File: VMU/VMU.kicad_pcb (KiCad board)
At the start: 4 copper layers, 76.2 x 53.3 mm, 62 parts, among them J1 TBL009-254-14GY-2GY, J2 TBL009-254-14GY-2GY, J3 Conn_01x08_Pin, J4 Conn_01x08_Pin, J5 Conn_01x02_Pin, J6 TBL009-254-14GY-2GY, J7 TBL009-254-14GY-2GY, J8 ARM_JTAG_SWD_10, Q1 NMOS, Q2 NMOS, Q3 NMOS, Q4 NMOS, Q6 NMOS, Q7 NMOS, U1 TLV9064, U2 TLV9064, U3 ADP150AUJZ-3.3-R7, U4 SN65HVD233, U5 STM32F091RCTx

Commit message: Labels
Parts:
- added G***: LOGO, LOGO, F.Cu at (127.0, 94.2)
- moved J5 2.25 mm to (104.5, 112.0)
- moved F3 2.00 mm to (104.8, 115.0)
- renumbered PWR to locked
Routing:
- net /PB_SUPPLY: track 58.5 -> 52.4 mm
- net GND: track 84.5 -> 81.5 mm
- net +5V: track 43.0 -> 41.2 mm

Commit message: Update
+ GND  vias
less silk screen
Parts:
- Hrt Beat: renamed from D6
- PB Supply: renamed from J5
- moved C2 1.25 mm to (141.5, 96.5)
- moved C1 1.00 mm to (141.2, 108.5)
- renumbered D7 to Error, Q2 to Q1, Q4 to Q2, Q6 to Q3, Q7 to Q4, Q1 to Q5, Q3 to Q6, D5 to Warning
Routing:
- net /CAN1_L: track 54.0 -> 69.1 mm
- net /PB_SUPPLY: track 52.4 -> 58.7 mm
- net GND: track 81.5 -> 75.7 mm, vias 28 -> 179
- net +5V: track 41.2 -> 45.6 mm, vias 7 -> 8
- net /I2C_SCL: track 59.7 -> 60.6 mm
- net /ANALOG_7_SIGNAL: track 18.8 -> 19.6 mm
- net /ANALOG_5_SIGNAL: track 38.2 -> 37.5 mm
- net /MCU/ANALOG_1: track 22.5 -> 23.0 mm
- net /GPIO_GND_2: track 13.7 -> 14.2 mm
- net /DIGITAL_SUPPLY_1: track 93.5 -> 94.0 mm
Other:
- board text added: "DATA IN"
- board text added: "DATA OUT"
- board text added: "Termination - CAN"

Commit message: Update
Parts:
- HRT BEAT: renamed from Hrt Beat
- J5: renamed from PB Supply
- moved G*** 18.0 mm to (110.5, 101.5)
- renumbered Error to ERROR, Q5 to Q1, Q1 to Q2, Q6 to Q3, Q2 to Q4, Q3 to Q6, Q4 to Q7, Warning to WARNING
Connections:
- J2 pad 15: GND -> +24V
- J2 pad 16: GND -> +24V
- J2 pad 25: GND -> +3.3V
- J2 pad 26: GND -> +3.3V
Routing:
- net GND: track 75.7 -> 26.1 mm, vias 179 -> 190
- net +24V: track 99.2 -> 120.2 mm, vias 1 -> 2
- net +3.3V: track 49.9 -> 64.7 mm, vias 9 -> 10
- net /GPIO_GND_3: track 50.5 -> 52.1 mm
- net /SPI_MOSI: track 29.7 -> 30.4 mm
- net /CAN1_L: track 69.1 -> 69.7 mm
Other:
- outline, holes or cut-outs redrawn
- board text added: "Filip Svebeck Emil Tagesson"
- board text added: "VMU-V1.0"
- board text added: "emiltag@kth.se"
- board text added: "fsvebeck@kth.se"
- board text removed: "GPIO2"

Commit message: Update
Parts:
- locked: renamed from HRT BEAT
- renumbered WARNING to locked, ERROR to locked
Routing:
- net GND: vias 190 -> 189
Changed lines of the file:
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@@
     (property "ki_keywords" "LED diode")
     (attr smd)
-    (fp_text reference "WARNING" (at 4.165 0.05 90) (layer "F.SilkS")
+    (fp_text reference locked "WARNING" (at 4.165 0.05 90) (layer "F.SilkS")
         (effects (font (size 0.8 0.8) (thickness 0.15)))
     )
@@
       (net 41 "/MCU/swdio") (pinfunction "SWDIO/TMS") (pintype "bidirectional"))
     (pad "3" thru_hole circle (at -1.27 0.635 270) (size 1 1) (drill 0.7) (layers "*.Cu" "*.Mask")
-      (net 2 "GND") (pinfunction "GND") (pintype "power_in"))
+      (net 2 "GND") (pinfunction "GND") (pintype "power_in") (thermal_bridge_angle 90))
     (pad "4" thru_hole circle (at -1.27 -0.635 270) (size 1 1) (drill 0.7) (layers "*.Cu" "*.Mask")
       (net 42 "/MCU/swdclk") (pinfunction "SWDCLK/TCK") (pintype "output"))
@@
     (property "ki_keywords" "LED diode")
     (attr smd)
-    (fp_text reference "HRT BEAT" (at 4.125 0.076 90) (layer "F.SilkS")
+    (fp_text reference locked "HRT BEAT" (at 4.125 0.076 90) (layer "F.SilkS")
         (effects (font (size 0.8 0.8) (thickness 0.15)))
     )
@@
     (property "ki_keywords" "LED diode")
     (attr smd)
-    (fp_text reference "ERROR" (at 3.375 -0.002 90) (layer "F.SilkS")
+    (fp_text reference locked "ERROR" (at 3.375 -0.002 90) (layer "F.SilkS")
         (effects (font (size 0.9 0.9) (thickness 0.15)))
     )
@@
   (via (at 118 87.75) (size 0.8) (drill 0.4) (layers "F.Cu" "B.Cu") (free) (net 2))
   (via (at 117.25 108) (size 0.8) (drill 0.4) (layers "F.Cu" "B.Cu") (net 2))
-  (via (at 93.25 99.5) (size 0.8) (drill 0.4) (layers "F.Cu" "B.Cu") (free) (net 2))
+  (via (at 94.25 99.75) (size 0.8) (drill 0.4) (layers "F.Cu" "B.Cu") (free) (net 2))
   (via (at 101.5 120.75) (size 0.8) (drill 0.4) (layers "F.Cu" "B.Cu") (free) (net 2))
   (via (at 158.25 111.75) (size 0.8) (drill 0.4) (layers "F.Cu" "B.Cu") (net 2))
@@
   (via (at 124.25 123.25) (size 0.8) (drill 0.4) (layers "F.Cu" "B.Cu") (free) (net 2))
   (via (at 112 105) (size 0.8) (drill 0.4) (layers "F.Cu" "B.Cu") (free) (net 2))
-  (via (at 92.75 95.75) (size 0.8) (drill 0.4) (layers "F.Cu" "B.Cu") (free) (net 2))
+  (via (at 93.25 95.75) (size 0.8) (drill 0.4) (layers "F.Cu" "B.Cu") (free) (net 2))
   (via (at 157.5 126) (size 0.8) (drill 0.4) (layers "F.Cu" "B.Cu") (free) (net 2))
   (via (at 142.5 78) (size 0.8) (drill 0.4) (layers "F.Cu" "B.Cu") (free) (net 2))
@@
   (via (at 121.75 83.75) (size 0.8) (drill 0.4) (layers "F.Cu" "B.Cu") (free) (net 2))
   (via (at 102.75 99) (size 0.8) (drill 0.4) (layers "F.Cu" "B.Cu") (free) (net 2))
-  (via (at 93 97.25) (size 0.8) (drill 0.4) (layers "F.Cu" "B.Cu") (free) (net 2))
+  (via (at 93.25 98.25) (size 0.8) (drill 0.4) (layers "F.Cu" "B.Cu") (free) (net 2))
   (via (at 121.75 86.5) (size 0.8) (drill 0.4) (layers "F.Cu" "B.Cu") (free) (net 2))
   (via (at 106.25 125.75) (size 0.8) (drill 0.4) (layers "F.Cu" "B.Cu") (free) (net 2))
@@
   (via (at 160.25 121) (size 0.8) (drill 0.4) (layers "F.Cu" "B.Cu") (free) (net 2))
   (via (at 116.75 117.0255) (size 0.8) (drill 0.4) (layers "F.Cu" "B.Cu") (free) (net 2))
-  (via (at 95.75 99.75) (size 0.8) (drill 0.4) (layers "F.Cu" "B.Cu") (free) (net 2))
   (via (at 140 120.75) (size 0.8) (drill 0.4) (layers "F.Cu" "B.Cu") (free) (net 2))
   (via (at 103.25 101) (size 0.8) (drill 0.4) (layers "F.Cu" "B.Cu") (free) (net 2))
@@
   (segment (start 134.52 85.83) (end 134.5 94.25) (width 0.25) (layer "B.Cu") (net 4))
   (segment (start 133.77 80) (end 133.77 85.08) (width 0.5) (layer "B.Cu") (net 4))
-  (segment (start 134.5 94.25) (end 134.52 94) (width 0.25) (layer "B.Cu") (net 4))
   (segment (start 133.77 85.08) (end 134.52 85.83) (width 0.25) (layer "B.Cu") (net 4))
   (segment (start 103.75 115.025) (end 103.725 115) (width 0.5) (layer "F.Cu") (net 5))

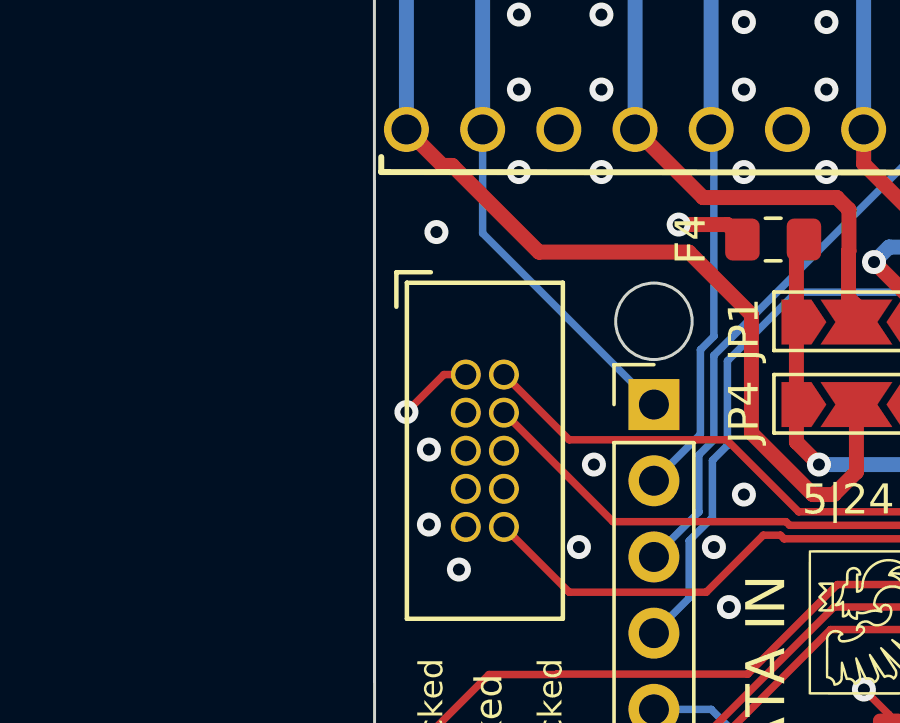
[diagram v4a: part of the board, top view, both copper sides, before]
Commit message: Footprint changes
annular holewidth
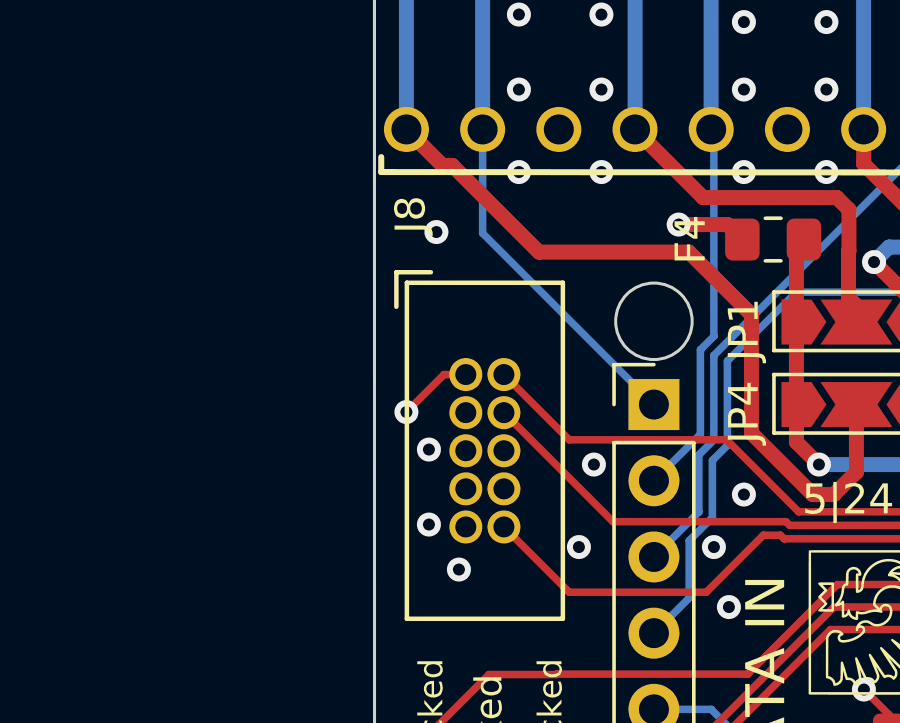
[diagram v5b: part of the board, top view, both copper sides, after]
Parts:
- J8: footprint KTHFS:Atmel_ICP_connector -> KTHFS:Atmel_ICP_connector(Eurocircuits)
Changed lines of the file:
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@@
     )
   )
-  (footprint "KTHFS:Atmel_ICP_connector" (layer "F.Cu")
+  (footprint "KTHFS:Atmel_ICP_connector(Eurocircuits)" (layer "F.Cu")
     (at 95.115 95.79 -90)
     (property "Sheetfile" "MCU.kicad_sch")
     (property "Sheetname" "MCU")
     (attr through_hole)
-    (fp_text reference "J8" (at 7.21 1.865 90) (layer "F.SilkS") hide
+    (fp_text reference "J8" (at -7.875 2.475 -270) (layer "F.SilkS")
         (effects (font (size 1 1) (thickness 0.15)))
     )
-    (fp_text value "ARM_JTAG_SWD_10" (at 6.5 0.95 90) (layer "F.Fab")
+    (fp_text value "ARM_JTAG_SWD_10" (at 6.5 0.95 -270) (layer "F.Fab")
         (effects (font (size 1 1) (thickness 0.15)))
     )
@@
     (fp_line (start 5.6 2.6) (end -5.6 2.6)
       (stroke (width 0.15) (type solid)) (layer "F.SilkS"))
-    (pad "1" thru_hole circle (at -2.54 0.635 270) (size 1 1) (drill 0.7) (layers "*.Cu" "*.Mask")
-      (net 4 "+3.3V") (pinfunction "VTref") (pintype "power_in"))
-    (pad "2" thru_hole circle (at -2.54 -0.635 270) (size 1 1) (drill 0.7) (layers "*.Cu" "*.Mask")
-      (net 41 "/MCU/swdio") (pinfunction "SWDIO/TMS") (pintype "bidirectional"))
-    (pad "3" thru_hole circle (at -1.27 0.635 270) (size 1 1) (drill 0.7) (layers "*.Cu" "*.Mask")
-      (net 2 "GND") (pinfunction "GND") (pintype "power_in") (thermal_bridge_angle 90))
-    (pad "4" thru_hole circle (at -1.27 -0.635 270) (size 1 1) (drill 0.7) (layers "*.Cu" "*.Mask")
-      (net 42 "/MCU/swdclk") (pinfunction "SWDCLK/TCK") (pintype "output"))
-    (pad "5" thru_hole circle (at 0 0.635 270) (size 1 1) (drill 0.7) (layers "*.Cu" "*.Mask")
-      (net 2 "GND") (pinfunction "GND") (pintype "passive") (thermal_bridge_angle 90))
-    (pad "6" thru_hole circle (at 0 -0.635 270) (size 1 1) (drill 0.7) (layers "*.Cu" "*.Mask")
-      (net 97 "unconnected-(J8-SWO{slash}TDO-Pad6)") (pinfunction "SWO/TDO") (pintype "input+no_connect"))
-    (pad "7" thru_hole circle (at 1.27 0.635 270) (size 1 1) (drill 0.7) (layers "*.Cu" "*.Mask")
-      (net 98 "unconnected-(J8-KEY-Pad7)") (pinfunction "KEY") (pintype "no_connect"))
-    (pad "8" thru_hole circle (at 1.27 -0.635 270) (size 1 1) (drill 0.7) (layers "*.Cu" "*.Mask")
-      (net 99 "unconnected-(J8-NC{slash}TDI-Pad8)") (pinfunction "NC/TDI") (pintype "output+no_connect"))
-    (pad "9" thru_hole circle (at 2.54 0.635 270) (size 1 1) (drill 0.7) (layers "*.Cu" "*.Mask")
-      (net 2 "GND") (pinfunction "GNDDetect") (pintype "passive") (thermal_bridge_angle 90))
-    (pad "10" thru_hole circle (at 2.54 -0.635 270) (size 1 1) (drill 0.7) (layers "*.Cu" "*.Mask")
-      (net 10 "/MCU/~{reset}") (pinfunction "~{RESET}") (pintype "open_collector"))
+    (pad "1" thru_hole circle (at -2.54 0.635 270) (size 1.1 1.1) (drill 0.7) (layers "*.Cu" "*.Mask")
+      (net 4 "+3.3V") (pinfunction "VTref") (pintype "power_in") (clearance 0.15) (thermal_bridge_angle 90))
+    (pad "2" thru_hole circle (at -2.54 -0.635 270) (size 1.1 1.1) (drill 0.7) (layers "*.Cu" "*.Mask")
+      (net 41 "/MCU/swdio") (pinfunction "SWDIO/TMS") (pintype "bidirectional") (clearance 0.15))
+    (pad "3" thru_hole circle (at -1.27 0.635 270) (size 1.1 1.1) (drill 0.7) (layers "*.Cu" "*.Mask")
+      (net 2 "GND") (pinfunction "GND") (pintype "power_in") (clearance 0.15))
+    (pad "4" thru_hole circle (at -1.27 -0.635 270) (size 1.1 1.1) (drill 0.7) (layers "*.Cu" "*.Mask")
+      (net 42 "/MCU/swdclk") (pinfunction "SWDCLK/TCK") (pintype "output") (clearance 0.15))
+    (pad "5" thru_hole circle (at 0 0.635 270) (size 1.1 1.1) (drill 0.7) (layers "*.Cu" "*.Mask")
+      (net 2 "GND") (pinfunction "GND") (pintype "passive") (clearance 0.15))
+    (pad "6" thru_hole circle (at 0 -0.635 270) (size 1.1 1.1) (drill 0.7) (layers "*.Cu" "*.Mask")
+      (net 97 "unconnected-(J8-SWO{slash}TDO-Pad6)") (pinfunction "SWO/TDO") (pintype "input+no_connect") (clearance 0.15))
+    (pad "7" thru_hole circle (at 1.27 0.635 270) (size 1.1 1.1) (drill 0.7) (layers "*.Cu" "*.Mask")
+      (net 98 "unconnected-(J8-KEY-Pad7)") (pinfunction "KEY") (pintype "no_connect") (clearance 0.15))
+    (pad "8" thru_hole circle (at 1.27 -0.635 270) (size 1.1 1.1) (drill 0.7) (layers "*.Cu" "*.Mask")
+      (net 99 "unconnected-(J8-NC{slash}TDI-Pad8)") (pinfunction "NC/TDI") (pintype "output+no_connect") (clearance 0.15))
+    (pad "9" thru_hole circle (at 2.54 0.635 270) (size 1.1 1.1) (drill 0.7) (layers "*.Cu" "*.Mask")
+      (net 2 "GND") (pinfunction "GNDDetect") (pintype "passive") (clearance 0.15))
+    (pad "10" thru_hole circle (at 2.54 -0.635 270) (size 1.1 1.1) (drill 0.7) (layers "*.Cu" "*.Mask")
+      (net 10 "/MCU/~{reset}") (pinfunction "~{RESET}") (pintype "open_collector") (clearance 0.15))
     (model "${KICAD_INFRASTRUCTURE}/libraries/3dmodels/Atmel_ICP_connector.stp"
       (offset (xyz -5.5 -2.5 0))

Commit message: update
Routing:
- net /CAN1_L: track 69.7 -> 54.6 mm
- net /CAN1_H: track 60.8 -> 59.7 mm
- net +5V: track 45.6 -> 46.5 mm
- net GND: track 26.1 -> 26.9 mm
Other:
- outline, holes or cut-outs redrawn
- board text added: "GPIO2"
- board text added: "Legend GND - Ground ADC - Analog signals SUP - Supply to sensors GPIO - Genreral Purpose I/O U_RX - UART RX U_TX - UART TX SCL - I2C SCL SDA - I2C SDA DSUP - Digital Supply ~{CS} - SPI ~{CS} SCLK - SPI SCLK MOSI - SPI MOSI MISO - SPI MISO CANH - CAN High CANL - CAN Low BATIN - Battery Input"

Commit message: Update
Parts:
- J8: footprint KTHFS:Atmel_ICP_connector(Eurocircuits) -> KTHFS:Atmel_ICP_connector
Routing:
- net +3.3V: track 64.4 -> 63.5 mm, vias 10 -> 9
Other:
- board text added: "Error"
- board text added: "Hrt Beat"
- board text added: "PB SUP"
- board text added: "PWR"
- board text added: "Warning"
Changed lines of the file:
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@@
     (property "ki_keywords" "LED diode")
     (attr smd)
-    (fp_text reference locked "WARNING" (at 4.165 0.05 90) (layer "F.SilkS")
+    (fp_text reference locked "D5" (at -0.335 1 90) (layer "F.SilkS") hide
         (effects (font (size 0.8 0.8) (thickness 0.15)))
     )
@@
     )
   )
-  (footprint "KTHFS:Atmel_ICP_connector(Eurocircuits)" (layer "F.Cu")
+  (footprint "KTHFS:Atmel_ICP_connector" (layer "F.Cu")
     (at 95.115 95.79 -90)
     (property "Sheetfile" "MCU.kicad_sch")
     (property "Sheetname" "MCU")
     (attr through_hole)
-    (fp_text reference "J8" (at -7.875 2.475 -270) (layer "F.SilkS")
+    (fp_text reference "J8" (at 6.71 1.365 -90) (layer "F.SilkS") hide
         (effects (font (size 1 1) (thickness 0.15)))
     )
-    (fp_text value "ARM_JTAG_SWD_10" (at 6.5 0.95 -270) (layer "F.Fab")
+    (fp_text value "ARM_JTAG_SWD_10" (at 6.5 0.95 -90) (layer "F.Fab")
         (effects (font (size 1 1) (thickness 0.15)))
     )
@@
     (property "ki_keywords" "LED diode")
     (attr smd)
-    (fp_text reference locked "HRT BEAT" (at 4.125 0.076 90) (layer "F.SilkS")
+    (fp_text reference locked "D6" (at 0.875 -2 90) (layer "F.SilkS") hide
         (effects (font (size 0.8 0.8) (thickness 0.15)))
     )
@@
     (property "ki_keywords" "connector")
     (attr through_hole)
-    (fp_text reference "J5" (at -2.25 1.275 90) (layer "F.SilkS")
+    (fp_text reference "J5" (at -2.25 1.025 90) (layer "F.SilkS") hide
         (effects (font (size 1 1) (thickness 0.15)))
     )
@@
     (property "ki_keywords" "LED diode")
     (attr smd)
-    (fp_text reference locked "ERROR" (at 3.375 -0.002 90) (layer "F.SilkS")
+    (fp_text reference locked "D7" (at 0.125 -0.75 90) (layer "F.SilkS") hide
         (effects (font (size 0.9 0.9) (thickness 0.15)))
     )
@@
     (property "ki_keywords" "LED diode")
     (attr smd)
-    (fp_text reference locked "PWR" (at -0.25 1.75 90) (layer "F.SilkS")
+    (fp_text reference locked "D4" (at -0.25 1.75 90) (layer "F.SilkS") hide
         (effects (font (size 1 1) (thickness 0.15)))
     )
@@
     (property "ki_keywords" "DC-DC, Step-down, Wurth")
     (attr through_hole)
-    (fp_text reference "VR1" (at 0.2125 1.6 90) (layer "F.SilkS")
+    (fp_text reference "VR1" (at 1.2125 1.0875 90) (layer "F.SilkS")
         (effects (font (size 1 1) (thickness 0.15)))
     )
@@
     (effects (font (size 1 1) (thickness 0.15)) (justify left bottom))
   )
+  (gr_text "PB SUP" (at 107.5 113.5 90) (layer "F.SilkS")
+    (effects (font (size 1 1) (thickness 0.15)) (justify left bottom))
+  )
   (gr_text "VMU-V1.0" (at 123.5 96 90) (layer "F.SilkS")
     (effects (font (size 1 1) (thickness 0.15)) (justify left bottom))
   )
+  (gr_text "Warning" (at 97.75 106.75 90) (layer "F.SilkS")
+    (effects (font (size 0.8 0.8) (thickness 0.1)) (justify left bottom))
+  )
   (gr_text "emiltag@kth.se" (at 130 97.25 90) (layer "F.SilkS")
     (effects (font (size 0.8 0.8) (thickness 0.15)) (justify left bottom))
@@
     (effects (font (size 1.3 1.3) (thickness 0.2)) (justify left bottom))
   )
+  (gr_text "Hrt Beat" (at 93.760639 106.749999 90) (layer "F.SilkS")
+    (effects (font (size 0.8 0.8) (thickness 0.1)) (justify left bottom))
+  )
+  (gr_text "Error" (at 95.75 106.75 90) (layer "F.SilkS")
+    (effects (font (size 0.8 0.8) (thickness 0.1)) (justify left bottom))
+  )
   (gr_text "fsvebeck@kth.se" (at 126.75 97.5 90) (layer "F.SilkS")
     (effects (font (size 0.8 0.8) (thickness 0.15)) (justify left bottom))
   )
+  (gr_text "PWR" (at 162.25 115.5 90) (layer "F.SilkS")
+    (effects (font (size 1 1) (thickness 0.15)) (justify left bottom))
+  )
   (gr_text "Termination - CAN" (at 136 88.25) (layer "F.SilkS")
     (effects (font (size 1 1) (thickness 0.2)) (justify left bottom))
@@
   (segment (start 108.5875 106.775) (end 108.5875 105.025) (width 0.5) (layer "F.Cu") (net 4))
   (segment (start 118 97.75) (end 118 98.8625) (width 0.25) (layer "F.Cu") (net 4))
-  (segment (start 93.75 93.25) (end 92.5 94.5) (width 0.25) (layer "F.Cu") (net 4))
   (segment (start 119.75 98.0375) (end 120.7125 98.0375) (width 0.25) (layer "F.Cu") (net 4))
   (segment (start 134.464 92.1245) (end 136.3955 92.1245) (width 0.5) (layer "F.Cu") (net 4))
@@
   (segment (start 129.834315 107) (end 128.65095 105.816635) (width 0.25) (layer "F.Cu") (net 4))
   (segment (start 118.5375 99.25) (end 119.75 98.0375) (width 0.5) (layer "F.Cu") (net 4))
-  (segment (start 94.48 93.25) (end 93.75 93.25) (width 0.25) (layer "F.Cu") (net 4))
   (segment (start 138.05 93.45) (end 137.25 94.25) (width 0.25) (layer "F.Cu") (net 4))
   (segment (start 131.1375 100.0375) (end 130.675 100.5) (width 0.25) (layer "F.Cu") (net 4))
@@
   (via (at 107 108.25) (size 0.8) (drill 0.4) (layers "F.Cu" "B.Cu") (net 4))
   (via (at 136 94.25) (size 0.8) (drill 0.4) (layers "F.Cu" "B.Cu") (net 4))
-  (via (at 92.5 94.5) (size 0.8) (drill 0.4) (layers "F.Cu" "B.Cu") (net 4))
   (via (at 107.75 103.75) (size 0.8) (drill 0.4) (layers "F.Cu" "B.Cu") (net 4))
   (via (at 132.25 98) (size 0.8) (drill 0.4) (layers "F.Cu" "B.Cu") (net 4))
@@
   (via (at 113.25 109.5) (size 0.8) (drill 0.4) (layers "F.Cu" "B.Cu") (net 4))
   (via (at 134.5 94.25) (size 0.8) (drill 0.4) (layers "F.Cu" "B.Cu") (net 4))
+  (segment (start 94.48 93.25) (end 94 93.25) (width 0.5) (layer "In2.Cu") (net 4))
+  (segment (start 94 93.25) (end 93.25 94) (width 0.5) (layer "In2.Cu") (net 4))
   (segment (start 134.52 85.83) (end 134.5 94.25) (width 0.25) (layer "B.Cu") (net 4))
   (segment (start 133.77 80) (end 133.77 85.08) (width 0.5) (layer "B.Cu") (net 4))
